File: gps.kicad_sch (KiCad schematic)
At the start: 22 parts, among them J6 SMA, J8 U.Fl, Q1 AO3400A, Q2 AO3401A, U1 MAX-M10S, U11 74LVC1G07

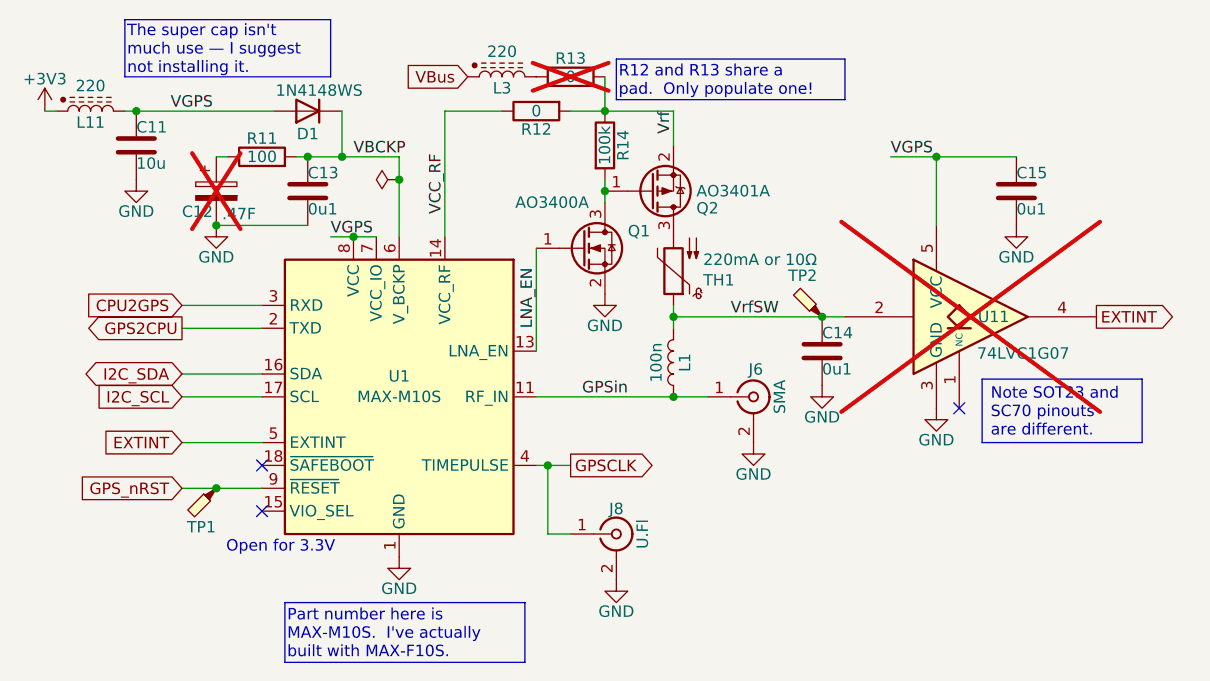
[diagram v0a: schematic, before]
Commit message: Remove unused components around GPS power.
(Ant. power switch & monitor, backup supercap.)
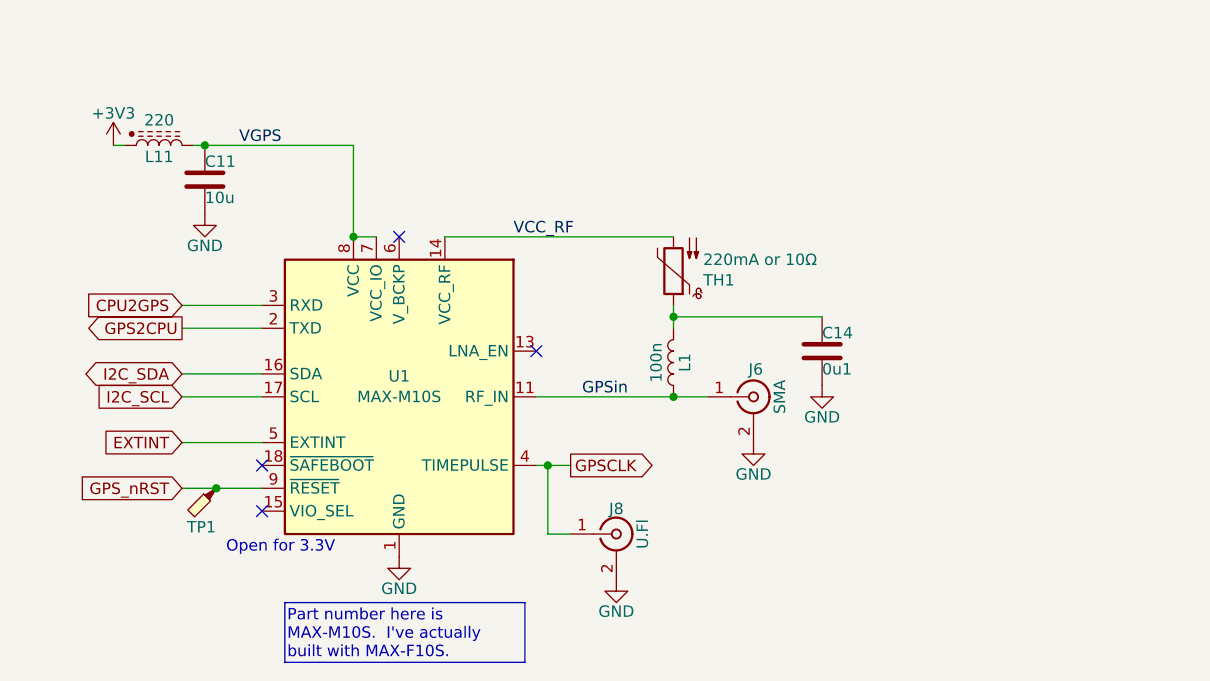
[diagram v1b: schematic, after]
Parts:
- removed C12: .47F, Parts:CP_Radial_D13.5mm_P5.00mm, symbol Device:C_Polarized
- removed C13, C15: 0u1, Capacitor_SMD:C_0402_1005Metric, symbol Device:C
- removed D1: 1N4148WS, Diode_SMD:D_SOD-323, symbol Diode:1N4148WS
- removed L3: 220, Inductor_SMD:L_0603_1608Metric, symbol Parts:L_Ferrite_Power
- removed Q1: AO3400A, Package_TO_SOT_SMD:SOT-23, symbol Transistor_FET:AO3400A
- removed Q2: AO3401A, Package_TO_SOT_SMD:SOT-23, symbol Transistor_FET:AO3401A
- removed R11: 100, Resistor_SMD:R_0402_1005Metric, symbol Device:R
- removed R12, R13: 0, Resistor_SMD:R_0603_1608Metric, symbol Device:R
- removed R14: 100k, Resistor_SMD:R_0402_1005Metric, symbol Device:R
- removed TP2: TestPoint_Probe, Parts:TestPoint, symbol Connector:TestPoint_Probe
- removed U11: 74LVC1G07, Parts:SOT-23-5, symbol 74xGxx:74LVC1G07
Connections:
- net VCC_RF: now also TH1.2
- net LNA_EN: no longer names the net of U1.13 (LNA_EN)
- net VBCKP: no longer names the net of U1.6 (V_BCKP)
- net VrfSW: no longer names the net of C14.1, L1.2, TH1.1
- no-connect marks 3 -> 4
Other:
- moved on the sheet: C11, L11

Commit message: FPGA in, layout mostly updated.
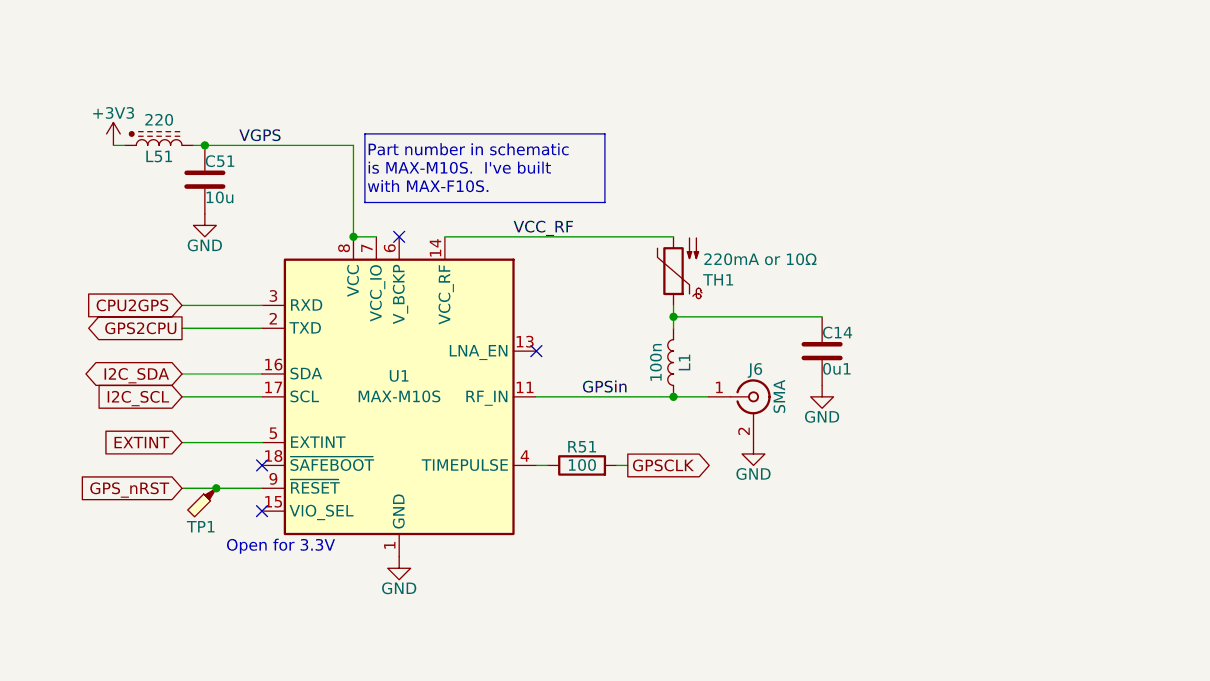
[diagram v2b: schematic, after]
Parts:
- removed J8: U.Fl, Parts:U.FL_Hirose_U.FL-R-SMT-1_Vertical, symbol Connector:Conn_Coaxial
- added R51: 100, Resistor_SMD:R_0402_1005Metric, symbol Device:R
- renumbered C11 to C51, L11 to L51
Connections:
- net GPSCLK: now also R51.2; no longer U1.4 (TIMEPULSE)
- new net: R51.1, U1.4 (TIMEPULSE)
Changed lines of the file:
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@@
 		)
 	)
-	(text_box "Part number here is MAX-M10S.  I've actually built with MAX-F10S."
+	(text_box "Part number in schematic is MAX-M10S.  I've built with MAX-F10S."
 		(exclude_from_sim no)
-		(at 87.63 121.92 0)
-		(size 26.67 6.6406)
+		(at 96.52 69.85 0)
+		(size 26.67 7.62)
 		(margins 0.254 0.254 0.254 0.254)
 		(stroke
@@
 	)
 	(junction
-		(at 116.84 106.68)
-		(diameter 0)
-		(color 0 0 0 0)
-	)
-	(junction
 		(at 95.25 81.28)
 		(diameter 0)
@@
 	(wire
 		(pts
+			(xy 80.01 109.22) (xy 85.09 109.22)
+		)
+		(stroke
+			(width 0)
+			(type default)
+		)
+	)
+	(wire
+		(pts
+			(xy 76.2 96.52) (xy 85.09 96.52)
+		)
+		(stroke
+			(width 0)
+			(type default)
+		)
+	)
+	(wire
+		(pts
+			(xy 130.81 90.17) (xy 147.32 90.17)
+		)
+		(stroke
+			(width 0)
+			(type default)
+		)
+	)
+	(wire
+		(pts
+			(xy 76.2 91.44) (xy 85.09 91.44)
+		)
+		(stroke
+			(width 0)
+			(type default)
+		)
+	)
+	(wire
+		(pts
+			(xy 115.57 99.06) (xy 130.81 99.06)
+		)
+		(stroke
+			(width 0)
+			(type default)
+		)
+	)
+	(wire
+		(pts
+			(xy 76.2 109.22) (xy 80.01 109.22)
+		)
+		(stroke
+			(width 0)
+			(type default)
+		)
+	)
+	(wire
+		(pts
 			(xy 115.57 106.68) (xy 116.84 106.68)
 		)
@@
 	(wire
 		(pts
-			(xy 80.01 109.22) (xy 85.09 109.22)
-		)
-		(stroke
-			(width 0)
-			(type default)
-		)
-	)
-	(wire
-		(pts
-			(xy 76.2 96.52) (xy 85.09 96.52)
-		)
-		(stroke
-			(width 0)
-			(type default)
-		)
-	)
-	(wire
-		(pts
-			(xy 130.81 90.17) (xy 147.32 90.17)
-		)
-		(stroke
-			(width 0)
-			(type default)
-		)
-	)
-	(wire
-		(pts
-			(xy 76.2 91.44) (xy 85.09 91.44)
-		)
-		(stroke
-			(width 0)
-			(type default)
-		)
-	)
-	(wire
-		(pts
-			(xy 115.57 99.06) (xy 130.81 99.06)
-		)
-		(stroke
-			(width 0)
-			(type default)
-		)
-	)
-	(wire
-		(pts
-			(xy 76.2 109.22) (xy 80.01 109.22)
-		)
-		(stroke
-			(width 0)
-			(type default)
-		)
-	)
-	(wire
-		(pts
-			(xy 116.84 114.3) (xy 116.84 106.68)
-		)
-		(stroke
-			(width 0)
-			(type default)
-		)
-	)
-	(wire
-		(pts
-			(xy 116.84 106.68) (xy 119.38 106.68)
-		)
-		(stroke
-			(width 0)
-			(type default)
-		)
-	)
-	(wire
-		(pts
 			(xy 68.58 71.12) (xy 69.85 71.12)
 		)
@@
 	(wire
 		(pts
-			(xy 116.84 114.3) (xy 119.38 114.3)
-		)
-		(stroke
-			(width 0)
-			(type default)
-		)
-	)
-	(wire
-		(pts
 			(xy 130.81 90.17) (xy 130.81 91.44)
 		)
@@
 		(pts
 			(xy 78.74 71.12) (xy 95.25 71.12)
+		)
+		(stroke
+			(width 0)
+			(type default)
+		)
+	)
+	(wire
+		(pts
+			(xy 124.46 106.68) (xy 125.73 106.68)
 		)
 		(stroke
@@
 	(global_label "GPSCLK"
 		(shape output)
-		(at 119.38 106.68 0)
-		(fields_autoplaced yes)
+		(at 125.73 106.68 0)
 		(effects
 			(font
@@
 		)
 		(property "Intersheetrefs" "${INTERSHEET_REFS}"
-			(at 129.6828 106.68 0)
+			(at 135.5248 106.68 0)
 			(show_name no)
 			(do_not_autoplace no)
@@
 		(in_pos_files yes)
 		(dnp no)
-		(property "Reference" "L11"
+		(property "Reference" "L51"
 			(at 73.66 72.39 90)
 			(show_name no)
@@
 			(project "gpsfreak"
 				(path "/3160ff17-81c2-4674-af97-e8d9acaf6b65/69331f4b-e5ad-4452-8850-5c5a77857efb"
-					(reference "L11")
+					(reference "L51")
 					(unit 1)
 				)
@@
 		(in_pos_files yes)
 		(dnp no)
-		(property "Reference" "C11"
+		(property "Reference" "C51"
 			(at 78.74 73.66 0)
 			(show_name no)
@@
 			(project "gpsfreak"
 				(path "/3160ff17-81c2-4674-af97-e8d9acaf6b65/69331f4b-e5ad-4452-8850-5c5a77857efb"
-					(reference "C11")
+					(reference "C51")
 					(unit 1)
 				)
@@
 	)
 	(symbol
-		(lib_id "power:GND")
-		(at 124.46 119.38 0)
+		(lib_id "Device:R")
+		(at 120.65 106.68 90)
 		(unit 1)
 		(body_style 1)
@@
 		(in_pos_files yes)
 		(dnp no)
-		(property "Reference" "#PWR06"
-			(at 124.46 125.73 0)
-			(hide yes)
-			(show_name no)
-			(do_not_autoplace no)
-			(effects
-				(font
-					(size 1.27 1.27)
-				)
-			)
-		)
-		(property "Value" "GND"
-			(at 124.46 122.174 0)
-			(show_name no)
-			(do_not_autoplace no)
-			(effects
-				(font
-					(size 1.27 1.27)
-				)
-				(justify top)
-			)
-		)
-		(property "Footprint" ""
-			(at 124.46 119.38 0)
+		(property "Reference" "R51"
+			(at 120.65 104.648 90)
+			(show_name no)
+			(do_not_autoplace no)
+			(effects
+				(font
+					(size 1.27 1.27)
+				)
+			)
+		)
+		(property "Value" "100"
+			(at 120.65 106.68 90)
+			(show_name no)
+			(do_not_autoplace no)
+			(effects
+				(font
+					(size 1.27 1.27)
+				)
+			)
+		)
+		(property "Footprint" "Resistor_SMD:R_0402_1005Metric"
+			(at 120.65 108.458 90)
 			(hide yes)
 			(show_name no)
@@
 		)
 		(property "Datasheet" ""
-			(at 124.46 119.38 0)
-			(hide yes)
-			(show_name no)
-			(do_not_autoplace no)
-			(effects
-				(font
-					(size 1.27 1.27)
-				)
-			)
-		)
-		(property "Description" "Power symbol creates a global label with name \"GND\" , ground"
-			(at 124.46 119.38 0)
-			(hide yes)
-			(show_name no)
-			(do_not_autoplace no)
-			(effects
-				(font
-					(size 1.27 1.27)
-				)
-			)
+			(at 120.65 106.68 0)
+			(hide yes)
+			(show_name no)
+			(do_not_autoplace no)
+			(effects
+				(font
+					(size 1.27 1.27)
+				)
+			)
+		)
+		(property "Description" "Resistor"
+			(at 120.65 106.68 0)
+			(hide yes)
+			(show_name no)
+			(do_not_autoplace no)
+			(effects
+				(font
+					(size 1.27 1.27)
+				)
+			)
+		)
+		(property "LCSC" "C25076"
+			(at 120.65 106.68 90)
+			(hide yes)
+			(show_name no)
+			(do_not_autoplace no)
+			(effects
+				(font
+					(size 1.27 1.27)
+				)
+			)
+		)
+		(pin "2"
 		)
 		(pin "1"
@@
 			(project "gpsfreak"
 				(path "/3160ff17-81c2-4674-af97-e8d9acaf6b65/69331f4b-e5ad-4452-8850-5c5a77857efb"
-					(reference "#PWR06")
+					(reference "R51")
 					(unit 1)
 				)
@@
 					(unit 1)
 				)
-			)
-		)
-	)
-	(symbol
-		(lib_id "Connector:Conn_Coaxial")
-		(at 124.46 114.3 0)
-		(unit 1)
-		(body_style 1)
-		(exclude_from_sim no)
-		(in_bom no)
-		(on_board yes)
-		(in_pos_files yes)
-		(dnp no)
-		(property "Reference" "J8"
-			(at 124.46 111.506 0)
-			(show_name no)
-			(do_not_autoplace no)
-			(effects
-				(font
-					(size 1.27 1.27)
-				)
-			)
-		)
-		(property "Value" "U.Fl"
-			(at 127.381 114.3 90)
-			(show_name no)
-			(do_not_autoplace no)
-			(effects
-				(font
-					(size 1.27 1.27)
-				)
-			)
-		)
-		(property "Footprint" "Parts:U.FL_Hirose_U.FL-R-SMT-1_Vertical"
-			(at 124.46 114.3 0)
-			(hide yes)
-			(show_name no)
-			(do_not_autoplace no)
-			(effects
-				(font
-					(size 1.27 1.27)
-				)
-			)
-		)
-		(property "Datasheet" ""
-			(at 124.46 114.3 0)
-			(hide yes)
-			(show_name no)
-			(do_not_autoplace no)
-			(effects
-				(font
-					(size 1.27 1.27)
-				)
-			)
-		)
-		(property "Description" "coaxial connector (BNC, SMA, SMB, SMC, Cinch/RCA, LEMO, ...)"
-			(at 124.46 114.3 0)
-			(hide yes)
-			(show_name no)
-			(do_not_autoplace no)
-			(effects
-				(font
-					(size 1.27 1.27)
-				)
-			)
-		)
-		(pin "2"
-		)
-		(pin "1"
-		)
-		(instances
-			(project "gpsfreak"
-				(path "/3160ff17-81c2-4674-af97-e8d9acaf6b65/69331f4b-e5ad-4452-8850-5c5a77857efb"
-					(reference "J8")
-					(unit 1)
-				)

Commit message: Layout down
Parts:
- C14, C51, R51: Stock (none) -> Basic
- J6: Stock (none) -> AliX
- L1: value 100n -> 68n; Stock (none) -> ORDER; now left out of the parts list
- L51: value 220 -> 120; Stock (none) -> Basic
- TH1: Stock (none) -> Ok
- TP1: Stock (none) -> N/A
- U1: Stock (none) -> ORDER, 1; now left out of the parts list
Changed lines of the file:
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@@
+			)
+		)
+		(property "Stock" "N/A"
+			(at 80.01 109.22 0)
+			(hide yes)
+			(show_name no)
+			(do_not_autoplace no)
+			(effects
+				(font
+					(size 1.27 1.27)
+				)
 			)
 		)
@@
 			)
 		)
+		(property "Stock" "AliX"
+			(at 139.7 99.06 0)
+			(hide yes)
+			(show_name no)
+			(do_not_autoplace no)
+			(effects
+				(font
+					(size 1.27 1.27)
+				)
+			)
+		)
 		(pin "2"
 		)
@@
 			)
 		)
-		(property "Value" "220"
+		(property "Value" "120"
 			(at 73.66 68.326 90)
 			(show_name no)
@@
 		)
 		(property "LCSC" "C14709"
+			(at 73.66 71.12 90)
+			(hide yes)
+			(show_name no)
+			(do_not_autoplace no)
+			(effects
+				(font
+					(size 1.27 1.27)
+				)
+			)
+		)
+		(property "Stock" "Basic"
 			(at 73.66 71.12 90)
 			(hide yes)
@@
 			)
 		)
+		(property "Stock" "Basic"
+			(at 78.74 74.93 0)
+			(hide yes)
+			(show_name no)
+			(do_not_autoplace no)
+			(effects
+				(font
+					(size 1.27 1.27)
+				)
+			)
+		)
 		(pin "1"
 		)
@@
 			)
 		)
+		(property "Stock" "Ok"
+			(at 130.81 85.09 0)
+			(hide yes)
+			(show_name no)
+			(do_not_autoplace no)
+			(effects
+				(font
+					(size 1.27 1.27)
+				)
+			)
+		)
 		(pin "2"
 		)
@@
 		(body_style 1)
 		(exclude_from_sim no)
-		(in_bom yes)
+		(in_bom no)
 		(on_board yes)
 		(in_pos_files yes)
@@
 			)
 		)
-		(property "Value" "100n"
+		(property "Value" "68n"
 			(at 128.905 95.25 90)
 			(show_name no)
@@
 			)
 		)
-		(property "Datasheet" "LQW15AWR10J80D"
+		(property "Datasheet" "LQW15AW68N"
 			(at 130.81 95.25 0)
 			(hide yes)
@@
 		)
 		(property "LCSC" "C3224079"
+			(at 130.81 95.25 90)
+			(hide yes)
+			(show_name no)
+			(do_not_autoplace no)
+			(effects
+				(font
+					(size 1.27 1.27)
+				)
+			)
+		)
+		(property "Stock" "ORDER"
 			(at 130.81 95.25 90)
 			(hide yes)
@@
 		(body_style 1)
 		(exclude_from_sim no)
-		(in_bom yes)
+		(in_bom no)
 		(on_board yes)
 		(in_pos_files yes)
@@
 		)
 		(property "LCSC" "C4153167"
+			(at 100.33 99.06 0)
+			(hide yes)
+			(show_name no)
+			(do_not_autoplace no)
+			(effects
+				(font
+					(size 1.27 1.27)
+				)
+			)
+		)
+		(property "Stock" "ORDER, 1"
 			(at 100.33 99.06 0)
 			(hide yes)
@@
 			)
 		)
+		(property "Stock" "Basic"
+			(at 147.32 93.98 0)
+			(hide yes)
+			(show_name no)
+			(do_not_autoplace no)
+			(effects
+				(font
+					(size 1.27 1.27)
+				)
+			)
+		)
 		(pin "1"
 		)
@@
 			(at 120.65 106.68 90)
 			(hide yes)
+			(show_name no)
+			(do_not_autoplace no)
+			(effects
+				(font
+					(size 1.27 1.27)
+				)
+			)
+		)
+		(property "Stock" "Basic"
+			(at 120.65 106.68 90)
+			(hide yes)
